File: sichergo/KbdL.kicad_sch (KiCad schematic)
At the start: 29 parts, among them J1 Conn_01x04_Pin, SW1 SW_Push_DPDT, U1 AZ1117-3.3, U2 TPD4E05U06DQA, U3 YTS1C0033BBG01, U4 STM32F103C8Tx, Y1 Crystal_GND24

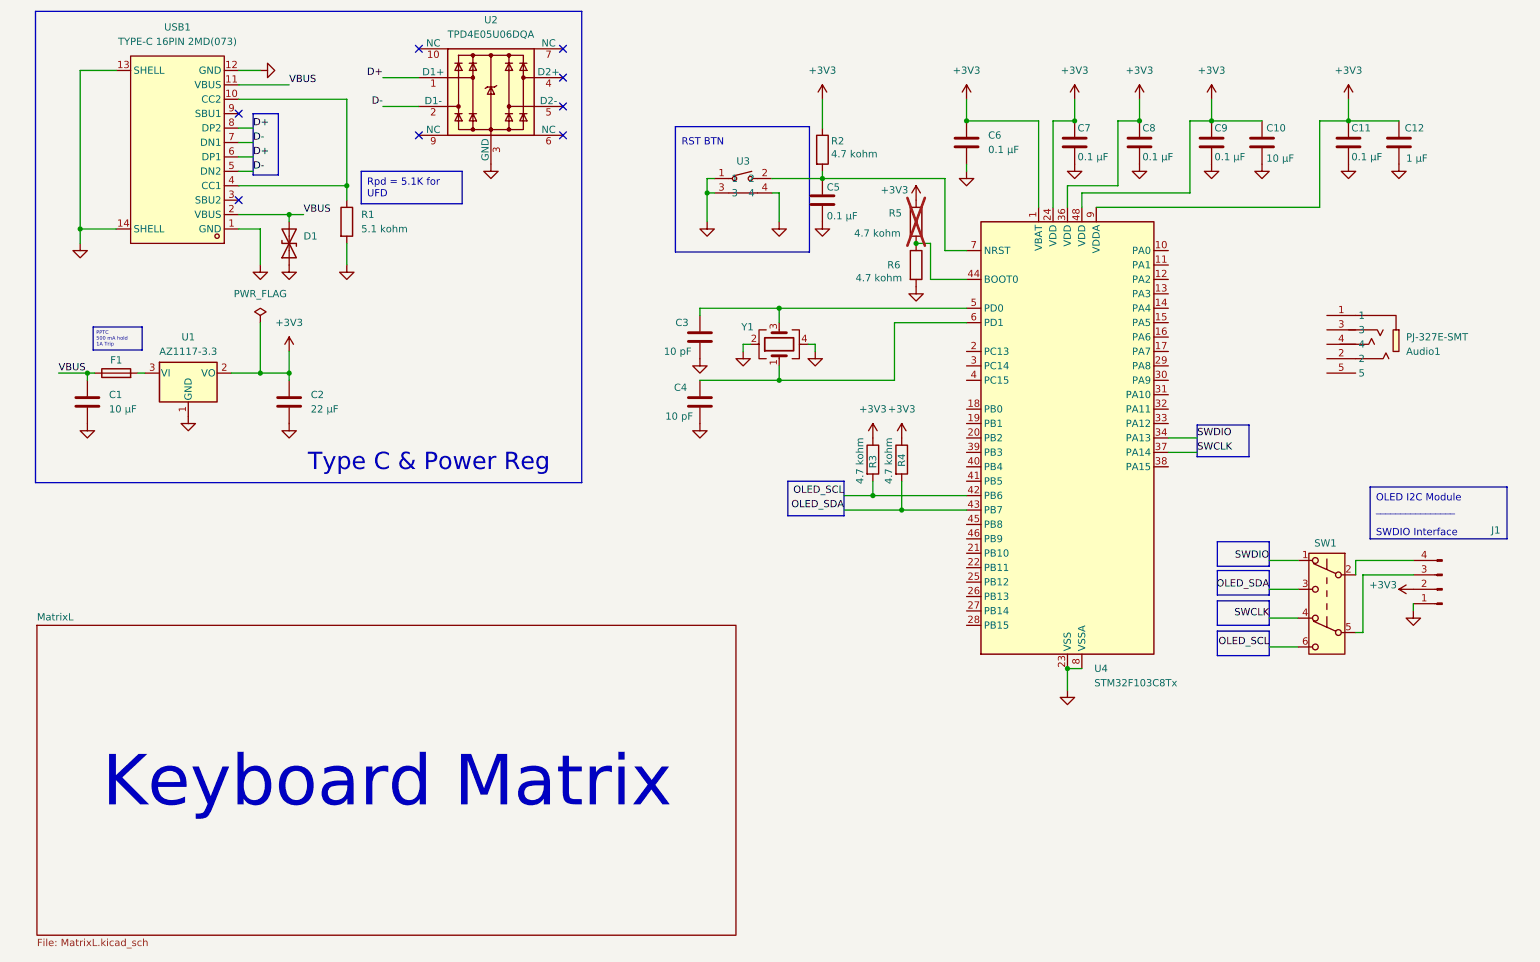
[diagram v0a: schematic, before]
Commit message: Added initial matrix and UART
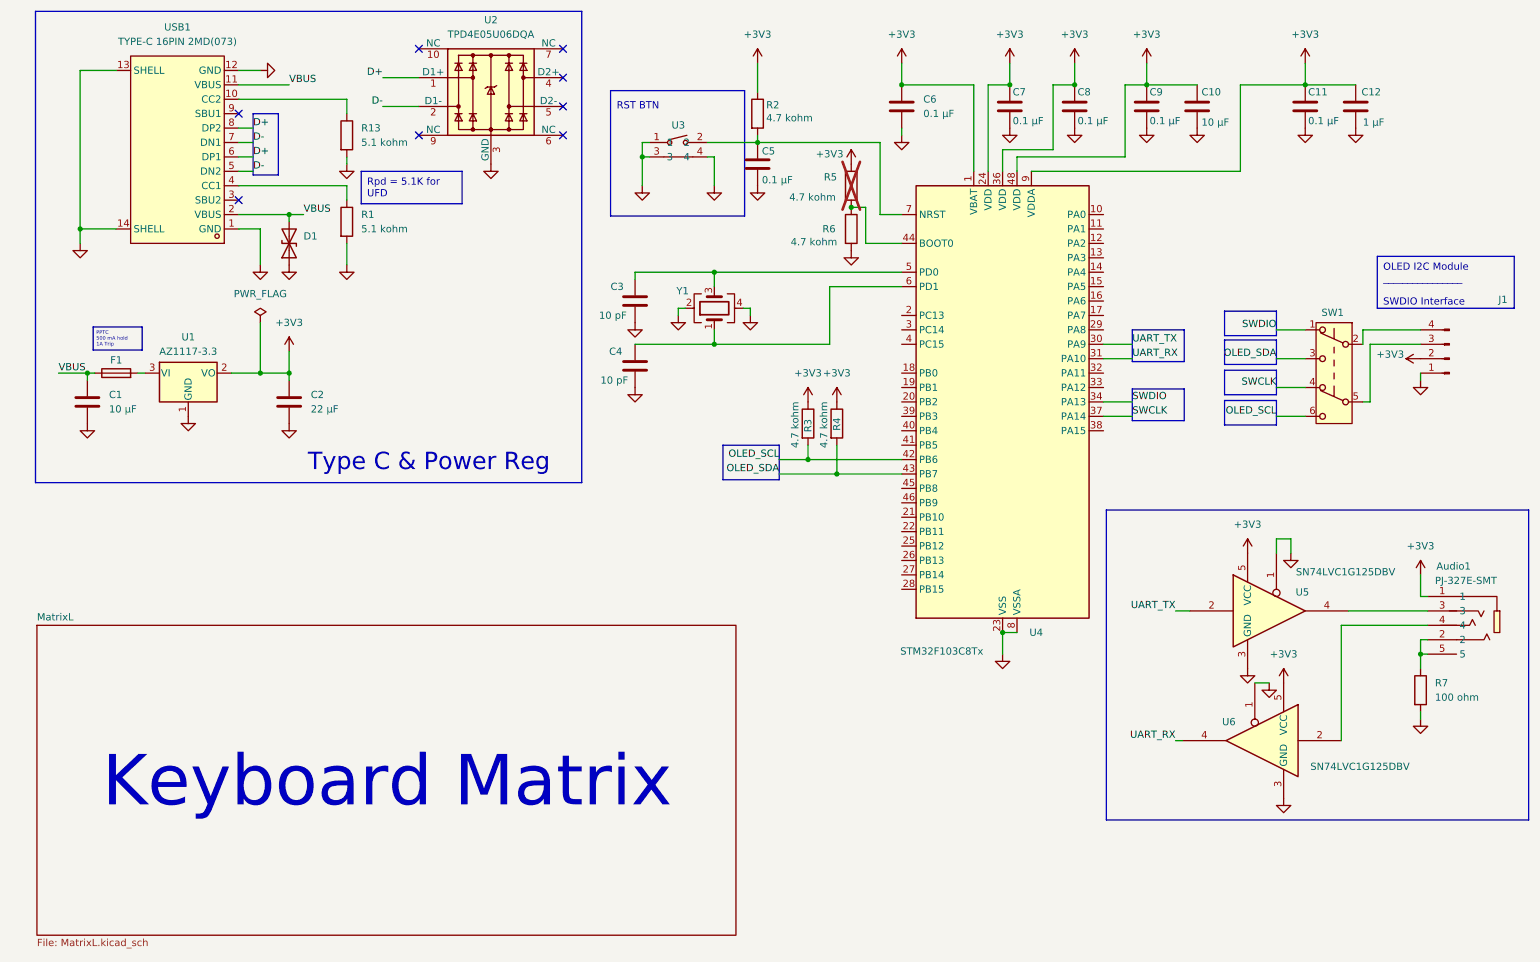
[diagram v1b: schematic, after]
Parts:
- added R13: 5.1 kohm, Resistor_SMD:R_0603_1608Metric_Pad0.98x0.95mm_HandSolder, symbol #inventree:RC0603FR-075K1L
- added R7: 100 ohm, Resistor_SMD:R_0805_2012Metric_Pad1.20x1.40mm_HandSolder, symbol #inventree:ERJ-6GEYJ101V
- added U5, U6: SN74LVC1G125DBV, Package_TO_SOT_SMD:SOT-23-5_HandSoldering, symbol 74xGxx:SN74LVC1G125DBV
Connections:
- net +3V3: now also Audio1.1, U5.5 (VCC), U6.5 (VCC)
- net GND: now also R13.2, R7.2, U5.1, U5.3 (GND), U6.1, U6.3 (GND)
- net at R1.1, USB1.4 (CC1): no longer USB1.10 (CC2)
- net UART_TX: now reaches U4.30 (PA9)
- net UART_TX: now also U5.2
- net UART_RX: now reaches U4.31 (PA10)
- net UART_RX: now also U6.4
- net at Audio1.2: now also Audio1.5, R7.1
- net at Audio1.3: now also U5.4
- net at Audio1.4: now also U6.2
- new net: R13.1, USB1.10 (CC2)
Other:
- moved on the sheet: C10, C11, C12, C3, C4, C5, C6, C7, C8, C9, J1, R2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

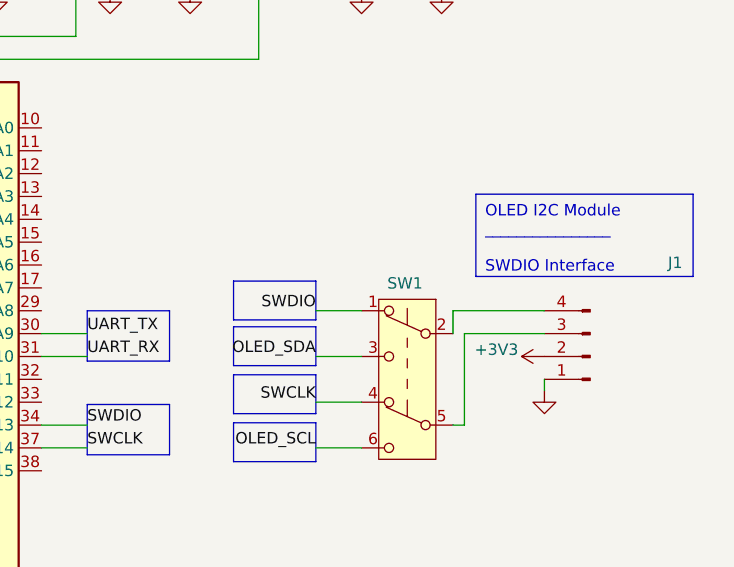
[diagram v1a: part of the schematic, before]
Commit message: Added footprints to switches
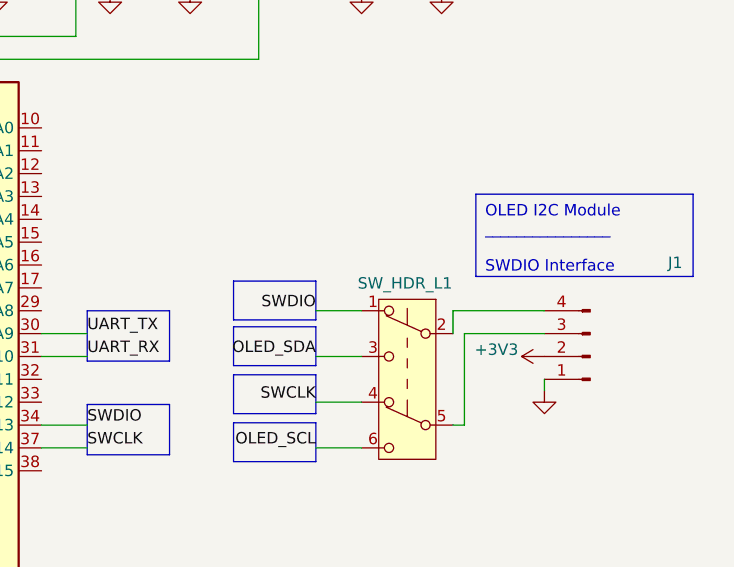
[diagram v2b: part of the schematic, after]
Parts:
- U5, U6: InvenTree (none) -> 66
- renumbered SW1 to SW_HDR_L1
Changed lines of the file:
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@@
 		(on_board yes)
 		(dnp no)
-		(property "Reference" "SW1"
+		(property "Reference" "SW_HDR_L1"
 			(at 248.666 70.612 0)
 			(effects
@@
 			(project "sichergo"
 				(path "/7d6715fb-1e77-4b7f-bc05-ec156d7f2ccd/83708fae-998d-4c1d-8b4c-c5f78cd3524c"
-					(reference "SW1")
+					(reference "SW_HDR_L1")
 					(unit 1)
 				)
@@
 			)
 		)
+		(property "InvenTree" "66"
+			(at 234.95 146.05 0)
+			(effects
+				(font
+					(size 1.27 1.27)
+				)
+				(hide yes)
+			)
+		)
 		(pin "1"
 		)
@@
 			(at 238.76 123.19 0)
 			(effects
+				(font
+					(size 1.27 1.27)
+				)
+				(hide yes)
+			)
+		)
+		(property "InvenTree" "66"
+			(at 238.76 123.19 0)
+			(effects

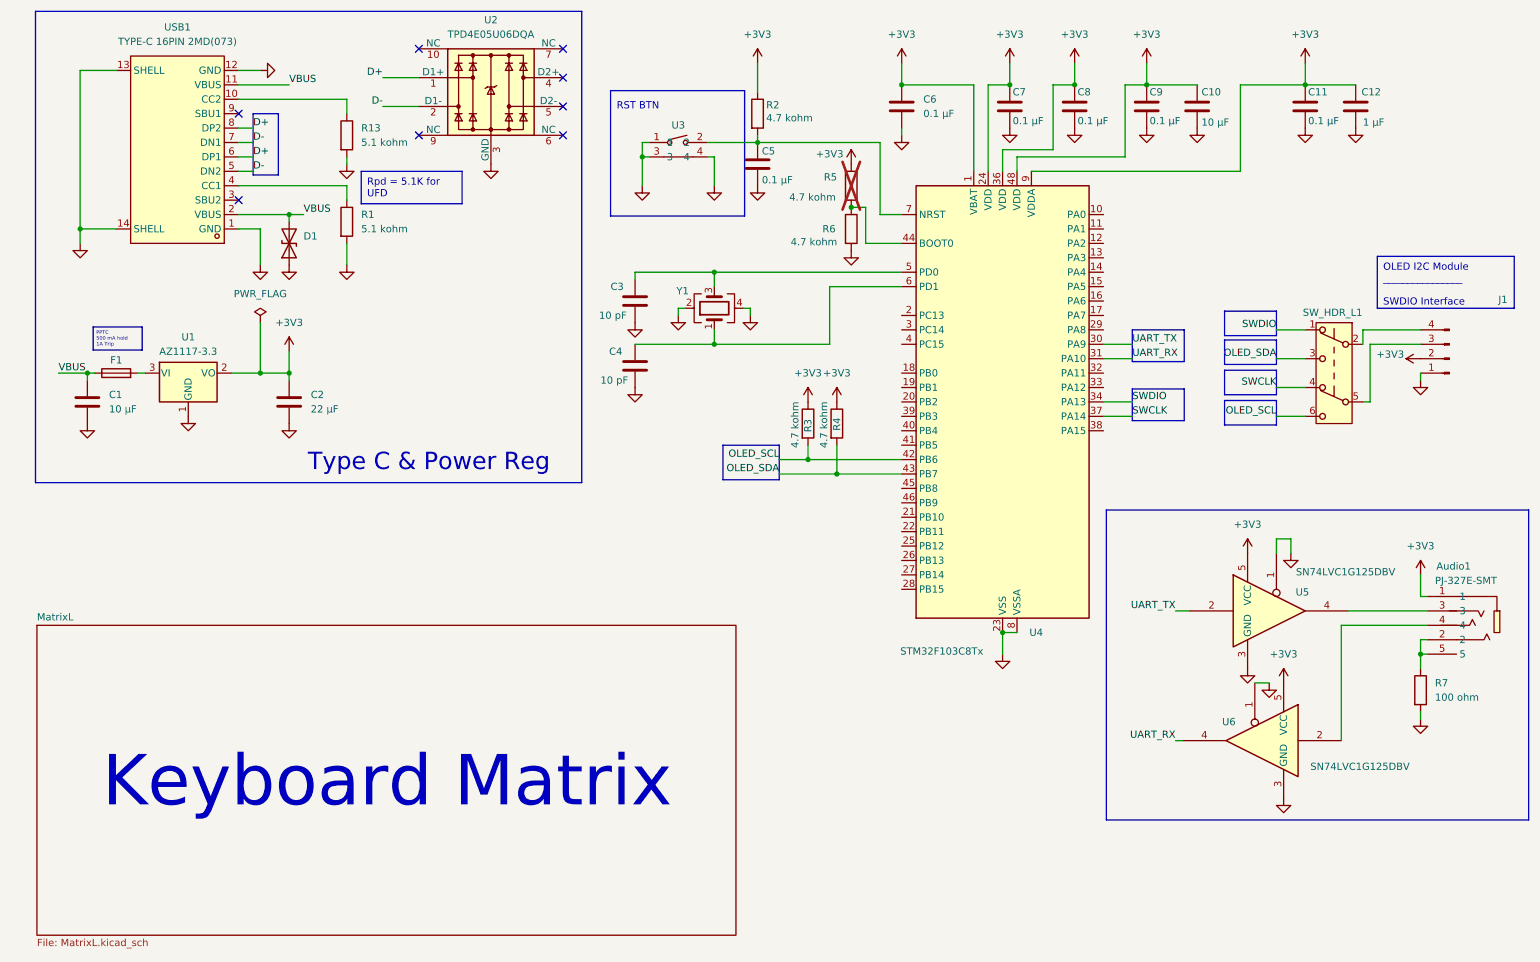
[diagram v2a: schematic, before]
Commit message: Add backlight and switch connections
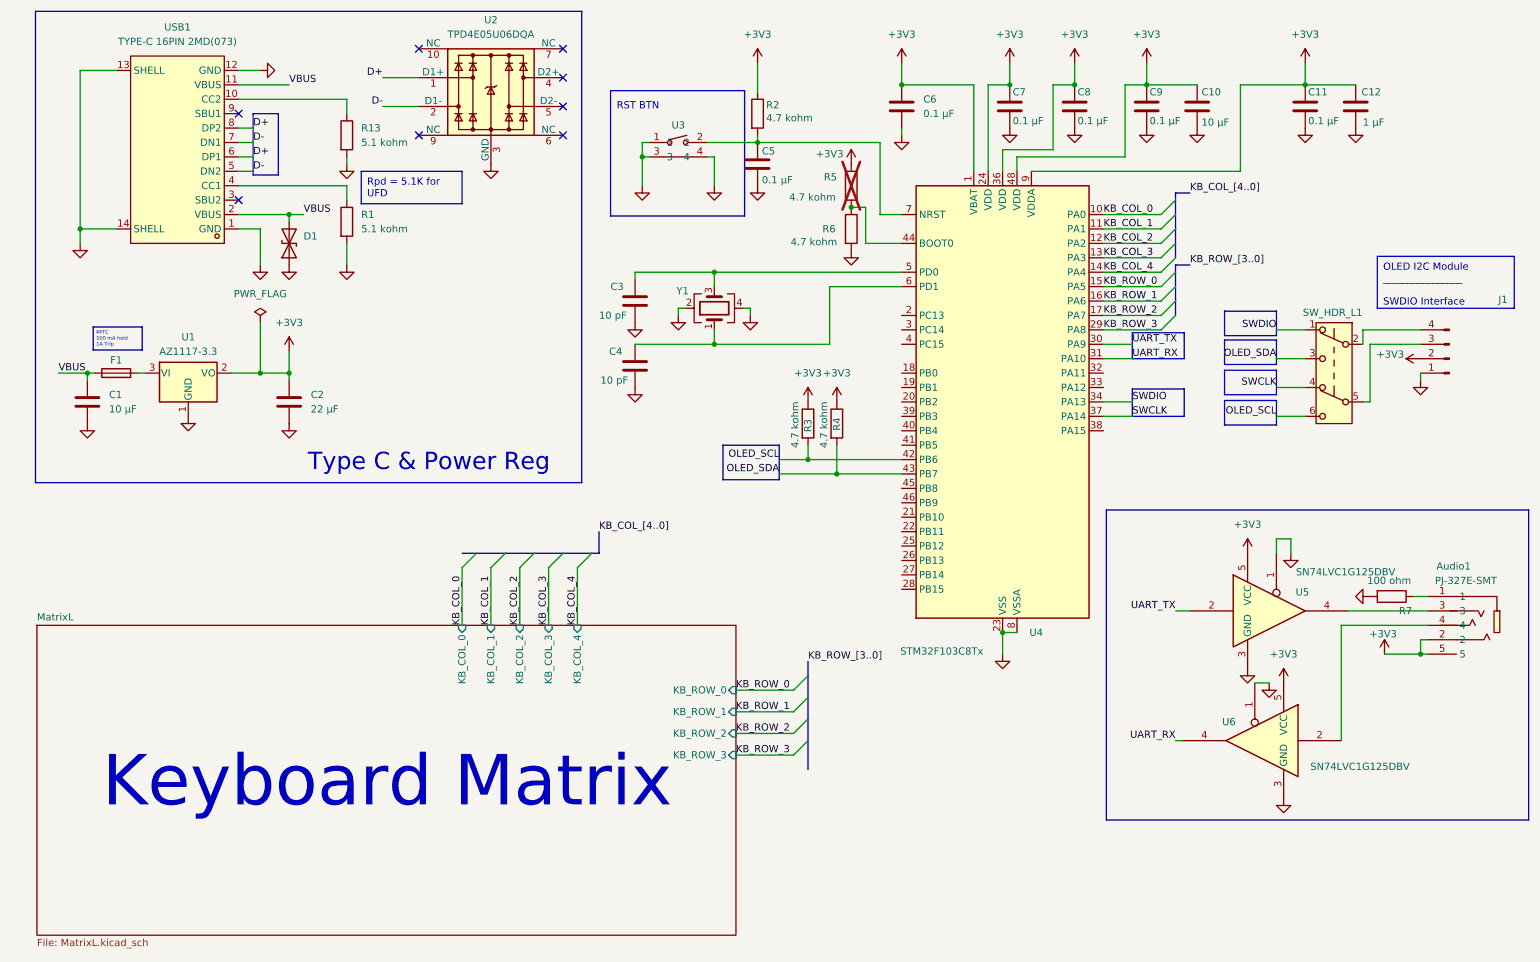
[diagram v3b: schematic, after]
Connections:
- net +3V3: now also Audio1.2, Audio1.5; no longer Audio1.1
- net KB_COL_0: now reaches U4.10 (PA0)
- net KB_COL_1: now reaches U4.11 (PA1)
- net KB_COL_2: now reaches U4.12 (PA2)
- net KB_COL_3: now reaches U4.13 (PA3)
- net KB_COL_4: now reaches U4.14 (PA4)
- net KB_ROW_0: now reaches U4.15 (PA5)
- net KB_ROW_1: now reaches U4.16 (PA6)
- net KB_ROW_2: now reaches U4.17 (PA7)
- net KB_ROW_3: now reaches U4.29 (PA8)
- new net: Audio1.1, R7.1
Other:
- sheet MatrixL ports: added KB_COL_0, KB_COL_1, KB_COL_2, KB_COL_3, KB_COL_4, KB_ROW_0, KB_ROW_1, KB_ROW_2, KB_ROW_3; removed none

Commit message: Pre finish layout
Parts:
- added Q2: 2N7002, Package_TO_SOT_SMD:SOT-23_Handsoldering, symbol Transistor_FET:2N7002
- added R51: 5.1 kohm, Resistor_SMD:R_0612_1632Metric_Pad1.18x3.40mm_HandSolder, symbol #inventree:RC0603FR-075K1L
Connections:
- net +3V3: now also Q2.3 (D)
- net GND: now also Q2.2 (S), R51.2
- net at U4.26 (PB13): now also Q2.1 (G), R51.1
- no-connect marks 8 -> 27
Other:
- sheet MatrixL ports: added LED_DRIVE; removed none

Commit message: Start layout
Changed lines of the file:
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@@
 	)
 	(junction
+		(at 63.5 30.48)
+		(diameter 0)
+		(color 0 0 0 0)
+	)
+	(junction
 		(at 147.32 40.64)
 		(diameter 0)
@@
 	)
 	(junction
-		(at 59.69 81.28)
-		(diameter 0)
-		(color 0 0 0 0)
-	)
-	(junction
 		(at 139.7 76.2)
 		(diameter 0)
@@
 	(wire
 		(pts
-			(xy 55.88 30.48) (xy 64.77 30.48)
+			(xy 55.88 30.48) (xy 63.5 30.48)
 		)
 		(stroke
@@
 	(wire
 		(pts
-			(xy 59.69 72.39) (xy 59.69 81.28)
-		)
-		(stroke
-			(width 0)
-			(type default)
-		)
-	)
-	(wire
-		(pts
 			(xy 115.57 115.57) (xy 115.57 125.73)
 		)
@@
 	(wire
 		(pts
-			(xy 59.69 81.28) (xy 64.77 81.28)
+			(xy 54.61 81.28) (xy 64.77 81.28)
 		)
 		(stroke
@@
 	(wire
 		(pts
-			(xy 54.61 81.28) (xy 59.69 81.28)
-		)
-		(stroke
-			(width 0)
-			(type default)
-		)
-	)
-	(wire
-		(pts
 			(xy 250.19 125.73) (xy 250.19 146.05)
 		)
@@
 	(wire
 		(pts
+			(xy 63.5 30.48) (xy 64.77 30.48)
+		)
+		(stroke
+			(width 0)
+			(type default)
+		)
+	)
+	(wire
+		(pts
 			(xy 193.04 43.18) (xy 212.09 43.18)
 		)
@@
 	(wire
 		(pts
+			(xy 63.5 24.13) (xy 63.5 30.48)
+		)
+		(stroke
+			(width 0)
+			(type default)
+		)
+	)
+	(wire
+		(pts
 			(xy 190.5 127) (xy 190.5 130.81)
 		)
@@
 	)
 	(symbol
+		(lib_id "power:PWR_FLAG")
+		(at 63.5 24.13 0)
+		(unit 1)
+		(exclude_from_sim no)
+		(in_bom yes)
+		(on_board yes)
+		(dnp no)
+		(fields_autoplaced yes)
+		(property "Reference" "#FLG01"
+			(at 63.5 22.225 0)
+			(effects
+				(font
+					(size 1.27 1.27)
+				)
+				(hide yes)
+			)
+		)
+		(property "Value" "PWR_FLAG"
+			(at 63.5 19.05 0)
+			(effects
+				(font
+					(size 1.27 1.27)
+				)
+			)
+		)
+		(property "Footprint" ""
+			(at 63.5 24.13 0)
+			(effects
+				(font
+					(size 1.27 1.27)
+				)
+				(hide yes)
+			)
+		)
+		(property "Datasheet" "~"
+			(at 63.5 24.13 0)
+			(effects
+				(font
+					(size 1.27 1.27)
+				)
+				(hide yes)
+			)
+		)
+		(property "Description" "Special symbol for telling ERC where power comes from"
+			(at 63.5 24.13 0)
+			(effects
+				(font
+					(size 1.27 1.27)
+				)
+				(hide yes)
+			)
+		)
+		(pin "1"
+		)
+		(instances
+			(project "sichergo"
+				(path "/7d6715fb-1e77-4b7f-bc05-ec156d7f2ccd/83708fae-998d-4c1d-8b4c-c5f78cd3524c"
+					(reference "#FLG01")
+					(unit 1)
+				)
+			)
+		)
+	)
+	(symbol
 		(lib_id "#inventree:CL21B104KBCNNNC")
 		(at 203.2 34.29 0)
@@
 					(unit 1)
 				)
-			)
-		)
-	)
-	(symbol
-		(lib_id "power:PWR_FLAG")
-		(at 59.69 72.39 0)
-		(unit 1)
-		(exclude_from_sim no)
-		(in_bom yes)
-		(on_board yes)
-		(dnp no)
-		(fields_autoplaced yes)
-		(property "Reference" "#FLG01"
-			(at 59.69 70.485 0)
-			(effects
-				(font
-					(size 1.27 1.27)
-				)
-				(hide yes)
-			)
-		)
-		(property "Value" "PWR_FLAG"
-			(at 59.69 67.31 0)
-			(effects
-				(font
-					(size 1.27 1.27)
-				)
-			)
-		)
-		(property "Footprint" ""
-			(at 59.69 72.39 0)
-			(effects
-				(font
-					(size 1.27 1.27)
-				)
-				(hide yes)
-			)
-		)
-		(property "Datasheet" "~"
-			(at 59.69 72.39 0)
-			(effects
-				(font
-					(size 1.27 1.27)
-				)
-				(hide yes)
-			)
-		)
-		(property "Description" "Special symbol for telling ERC where power comes from"
-			(at 59.69 72.39 0)
-			(effects
-				(font
-					(size 1.27 1.27)
-				)
-				(hide yes)
-			)
-		)
-		(pin "1"
-		)
-		(instances
-			(project "sichergo"
-				(path "/7d6715fb-1e77-4b7f-bc05-ec156d7f2ccd/83708fae-998d-4c1d-8b4c-c5f78cd3524c"
-					(reference "#FLG01")
-					(unit 1)
-				)
